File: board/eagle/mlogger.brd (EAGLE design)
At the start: 59.4 x 33.3 mm, 47 parts, among them J1 MICROSD-9P, SW1 SS-12D00G3, SW2 TVAF06-A020B-R, SW3 TVAF06-A020B-R

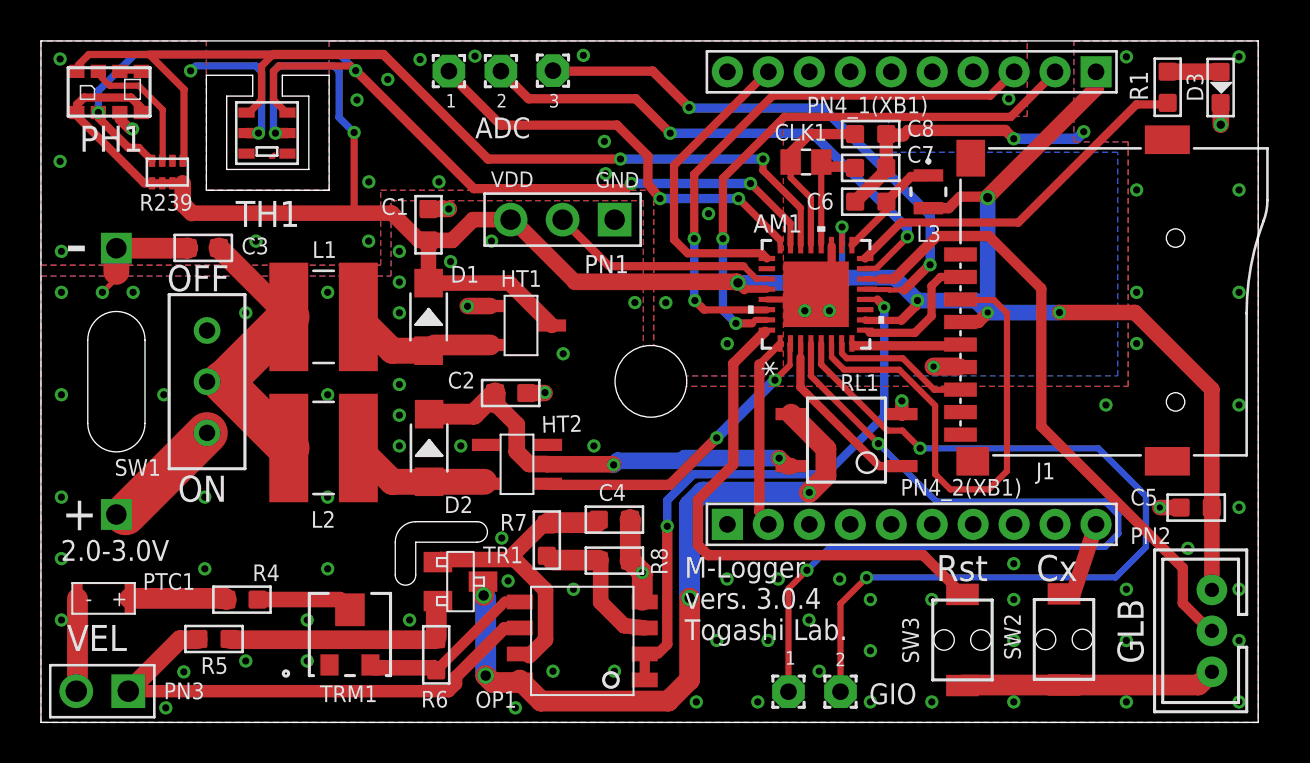
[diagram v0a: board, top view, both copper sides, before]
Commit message: アナログReference電圧に三端子レギュレータ回路を追加。
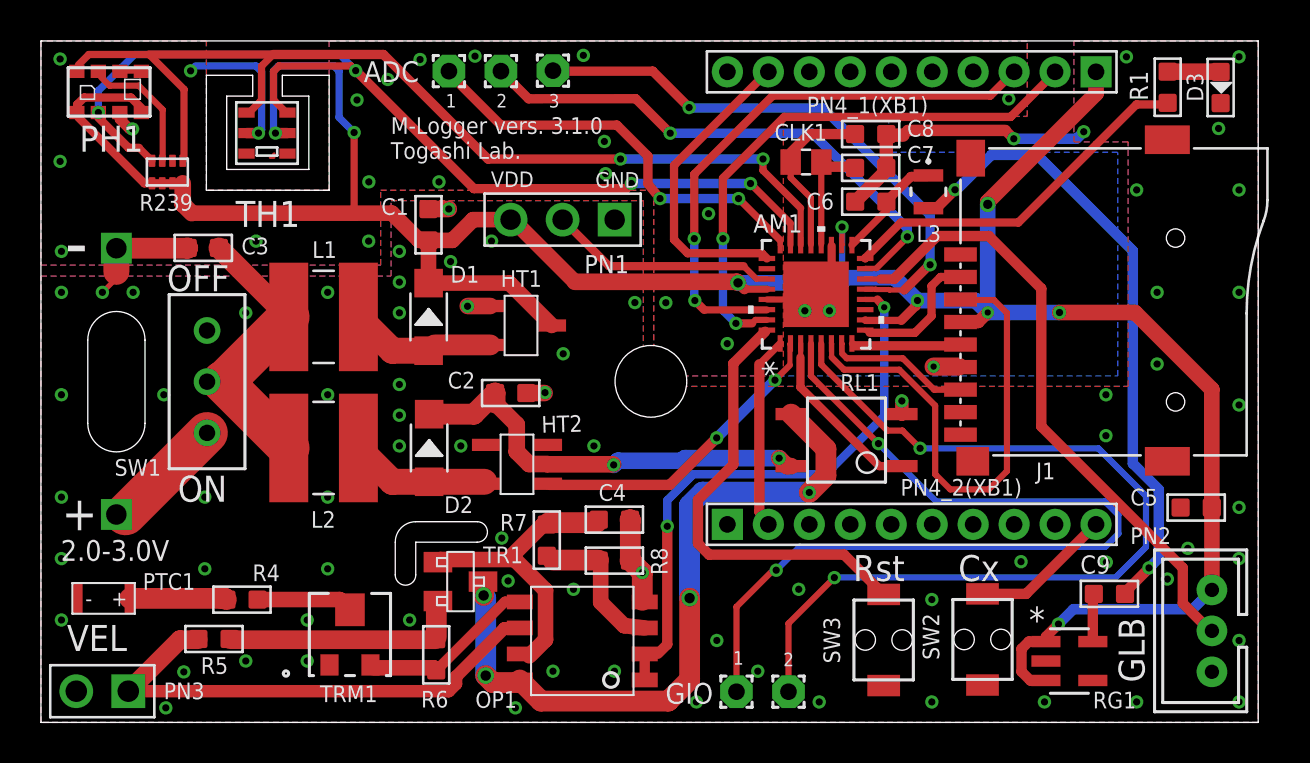
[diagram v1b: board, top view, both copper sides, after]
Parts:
- added C9: (no value), MyParts:C0603
- added RG1: TCR2EF20SOT-25___(SMV)_TOS, MyParts:SOT-25___(SMV)_TOS
- moved SW2 3.98 mm to (46.0, 4.05)
- moved SW3 3.85 mm to (41.1, 4.03)
- moved PAD3 2.54 mm to (36.5, 1.50)
- moved PAD4 2.54 mm to (34.0, 1.50)
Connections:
- new net N$7: C9.2, L3.2
- new net N$9: C9.1, RG1.5
- net GND: now also RG1.2
- net VDD: now also RG1.1, RG1.3; no longer L3.2
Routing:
- net N$7: track 0.00 -> 31.0 mm, vias 0 -> 2
- net GND: track 63.1 -> 44.0 mm, vias 107 -> 98
- net VDD: track 126.6 -> 136.6 mm, vias 8 -> 9
- net N$5: track 25.8 -> 21.9 mm
- net N$3: track 4.02 -> 6.95 mm
- net N$9: track 0.00 -> 2.35 mm
- net N$13: track 42.6 -> 44.6 mm
- net N$12: track 42.4 -> 44.4 mm
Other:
- board text added: "M-Logger vers. 3.1.0 Togashi Lab."
- board text removed: "M-Logger vers. 3.0.4 Togashi Lab."

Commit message: レギュレータの接続ミス修正
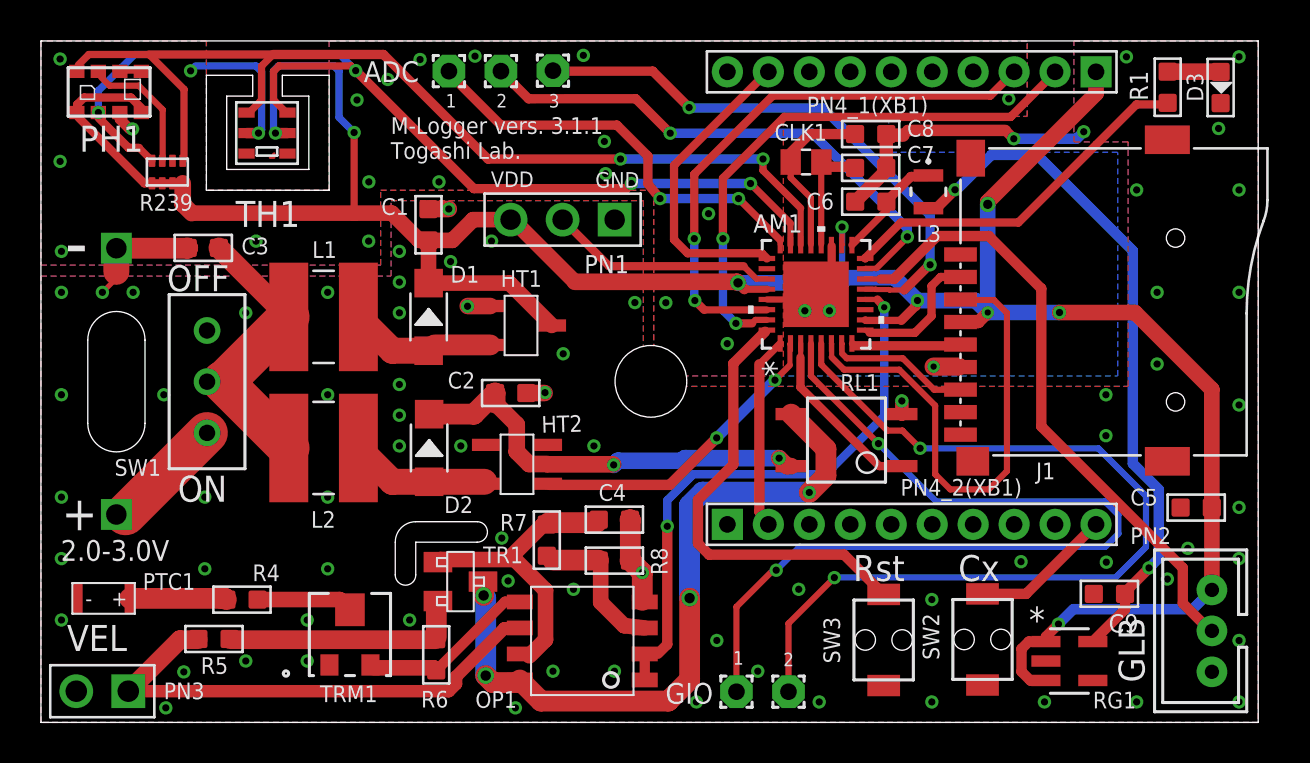
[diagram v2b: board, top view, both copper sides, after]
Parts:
- turned C9 to 270 degrees
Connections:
- removed net N$9: C9.1, RG1.5
- net GND: now also C9.2
- net N$7: now also C9.1, RG1.5; no longer C9.2
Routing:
- net N$7: track 31.0 -> 33.9 mm
- net N$9: track 2.35 -> 0.00 mm
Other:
- board text added: "M-Logger vers. 3.1.1 Togashi Lab."
- board text removed: "M-Logger vers. 3.1.0 Togashi Lab."
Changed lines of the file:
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@@
 <setting verticaltext="up"/>
 </settings>
-<grid distance="0.5" unitdist="mm" unit="mm" style="lines" multiple="1" display="yes" altdistance="1" altunitdist="mil" altunit="mil"/>
+<grid distance="19.6850394" unitdist="mil" unit="mil" style="lines" multiple="1" display="yes" altdistance="1" altunitdist="mil" altunit="mil"/>
 <layers>
 <layer number="1" name="Top" color="4" fill="1" visible="yes" active="yes"/>
@@
 <wire x1="59.436" y1="33.274" x2="0" y2="33.274" width="0" layer="20"/>
 <wire x1="0" y1="33.274" x2="0" y2="0" width="0" layer="20"/>
-<text x="17.08" y="27.5166" size="0.8128" layer="25" font="vector">M-Logger vers. 3.1.0
+<text x="17.08" y="27.5166" size="0.8128" layer="25" font="vector">M-Logger vers. 3.1.1
 Togashi Lab.</text>
 <circle x="29.718" y="16.637" radius="3.302" width="0.1524" layer="41"/>
@@
 <attribute name="NAME" x="51.3642" y="0.6858" size="0.8128" layer="25" ratio="6"/>
 </element>
-<element name="C9" library="MyParts" package="C0603" package3d_urn="urn:adsk.eagle:package:8004287/1" value="" x="52.1716" y="6.2738" smashed="yes" rot="R90">
-<attribute name="NAME" x="50.7492" y="7.2644" size="0.889" layer="25" ratio="11"/>
-<attribute name="NAME" x="50.9016" y="6.0198" size="0.635" layer="33" ratio="10"/>
-<attribute name="VALUE" x="50.9016" y="4.6863" size="0.635" layer="27" ratio="10"/>
+<element name="C9" library="MyParts" package="C0603" package3d_urn="urn:adsk.eagle:package:8004287/1" value="" x="52.1716" y="6.2738" smashed="yes" rot="R270">
+<attribute name="NAME" x="53.594" y="5.2832" size="0.889" layer="25" ratio="11" rot="R180"/>
+<attribute name="NAME" x="53.4416" y="6.5278" size="0.635" layer="33" ratio="10" rot="R180"/>
+<attribute name="VALUE" x="53.4416" y="7.8613" size="0.635" layer="27" ratio="10" rot="R180"/>
 </element>
 </elements>
@@
 <via x="57.5" y="29" extent="1-16" drill="0.35"/>
 <via x="55" y="7" extent="1-16" drill="0.35"/>
+<contactref element="C9" pad="2"/>
 </signal>
 <signal name="VDD" class="2">
@@
 </signal>
 <signal name="N$7">
+<contactref element="RG1" pad="5"/>
+<contactref element="C9" pad="1"/>
 <contactref element="L3" pad="2"/>
 <via x="54.102" y="7.5438" extent="1-16" drill="0.35"/>
@@
 <wire x1="44.6278" y1="26.0096" x2="43.7261" y2="25.1079" width="0.508" layer="1"/>
 <wire x1="43.7261" y1="25.1079" x2="43.3324" y2="25.1079" width="0.254" layer="1"/>
-<contactref element="C9" pad="2"/>
+<wire x1="54.102" y1="7.5438" x2="54.102" y2="7.5272" width="0.508" layer="1"/>
+<wire x1="52.9336" y1="6.3588" x2="54.102" y2="7.5272" width="0.508" layer="1"/>
+<wire x1="51.3602" y1="3.9472" x2="52.9336" y2="5.5206" width="0.508" layer="1"/>
+<wire x1="52.9336" y1="5.5206" x2="52.9336" y2="6.2738" width="0.508" layer="1"/>
 <wire x1="52.9336" y1="6.2738" x2="52.9336" y2="6.3588" width="0.254" layer="1"/>
-<wire x1="54.102" y1="7.5438" x2="54.102" y2="7.5272" width="0.508" layer="1"/>
-<wire x1="54.102" y1="7.5272" x2="52.9336" y2="6.3588" width="0.508" layer="1"/>
-</signal>
-<signal name="N$9">
-<contactref element="RG1" pad="5"/>
-<contactref element="C9" pad="1"/>
-<wire x1="51.3602" y1="3.9472" x2="51.3602" y2="6.2244" width="0.508" layer="1"/>
-<wire x1="51.3602" y1="6.2244" x2="51.4096" y2="6.2738" width="0.254" layer="1"/>
 </signal>
 </signals>

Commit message: GIOの間にGNDピンを追加。
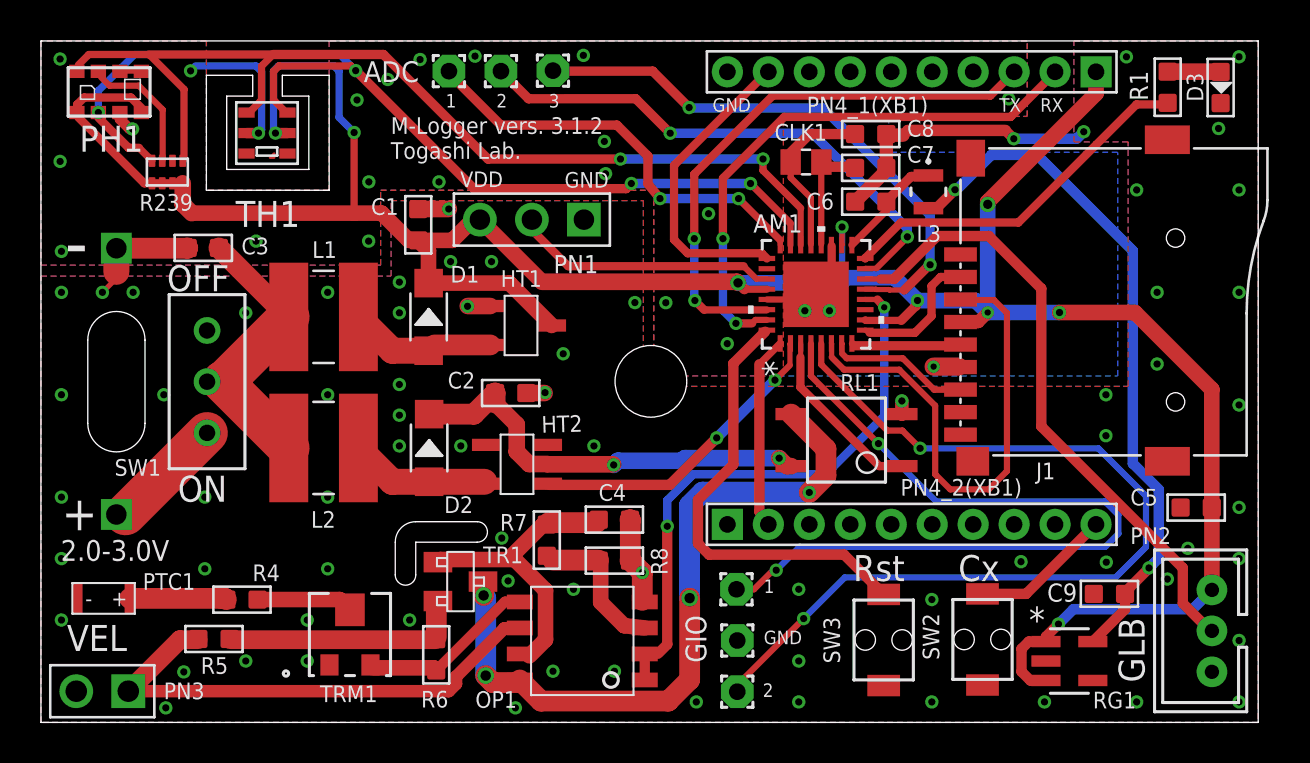
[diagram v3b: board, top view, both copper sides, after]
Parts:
- added PAD6: (no value), wirepad:1,6/0,8
- moved PAD4 5.00 mm to (34.0, 6.50)
- moved PAD3 2.50 mm to (34.0, 1.50)
- moved PN1 1.50 mm to (24.0, 24.5)
- moved C1 0.50 mm to (18.4, 24.3)
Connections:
- net GND: now also PAD6.1
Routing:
- net N$13: track 44.6 -> 40.1 mm
- net UPDI: track 11.2 -> 13.0 mm
- net N$12: track 44.4 -> 45.1 mm
- net GND: track 44.0 -> 44.5 mm, vias 98 -> 96
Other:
- board text added: "M-Logger vers. 3.1.2 Togashi Lab."
- board text added: "RX"
- board text added: "TX"
- board text removed: "M-Logger vers. 3.1.1 Togashi Lab."
